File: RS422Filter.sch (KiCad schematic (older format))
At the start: 26 parts

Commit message: start placement
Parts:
- C27, C28, C29, C30, C31, C32, C33, C34: renamed from C?; footprint (none) -> Capacitor_SMD:C_0603_1608Metric
- D19, D20: renamed from D?; footprint (none) -> Package_TO_SOT_SMD:SOT-23
- R61, R62, R63, R64, R65, R66: renamed from R?; footprint (none) -> Resistor_SMD:R_0603_1608Metric
- gave numbers to parts that had none: 10

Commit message: placement
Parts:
- removed C29, C30: 470p, Capacitor_SMD:C_0603_1608Metric, symbol AR2ISS:C
- removed C33, C34: 1n, Capacitor_SMD:C_0603_1608Metric, symbol AR2ISS:C
- removed D20: PESD2CAN, Package_TO_SOT_SMD:SOT-23, symbol Device:D_TVS_x2_AAC
- removed J13: Conn_01x02, symbol Connector_Generic:Conn_01x02
- removed L12, L13: 10u, symbol Device:L
- removed L16, L17: 74279266, symbol Device:L
- removed R63, R64: 221, Resistor_SMD:R_0603_1608Metric, symbol AR2ISS:R
- removed R66: 120, Resistor_SMD:R_0603_1608Metric, symbol AR2ISS:R
- D19: footprint Package_TO_SOT_SMD:SOT-23 -> Package_TO_SOT_SMD:SOT-23_Handsoldering
- J12: footprint (none) -> Connector_PinHeader_2.54mm:PinHeader_1x02_P2.54mm_Vertical
- L14, L15: footprint (none) -> Inductor_SMD:L_0603_1608Metric
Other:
- moved on the sheet: C14, C15, C18, C19, D17, J9, L1, L2, L5, L6, R36, R37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

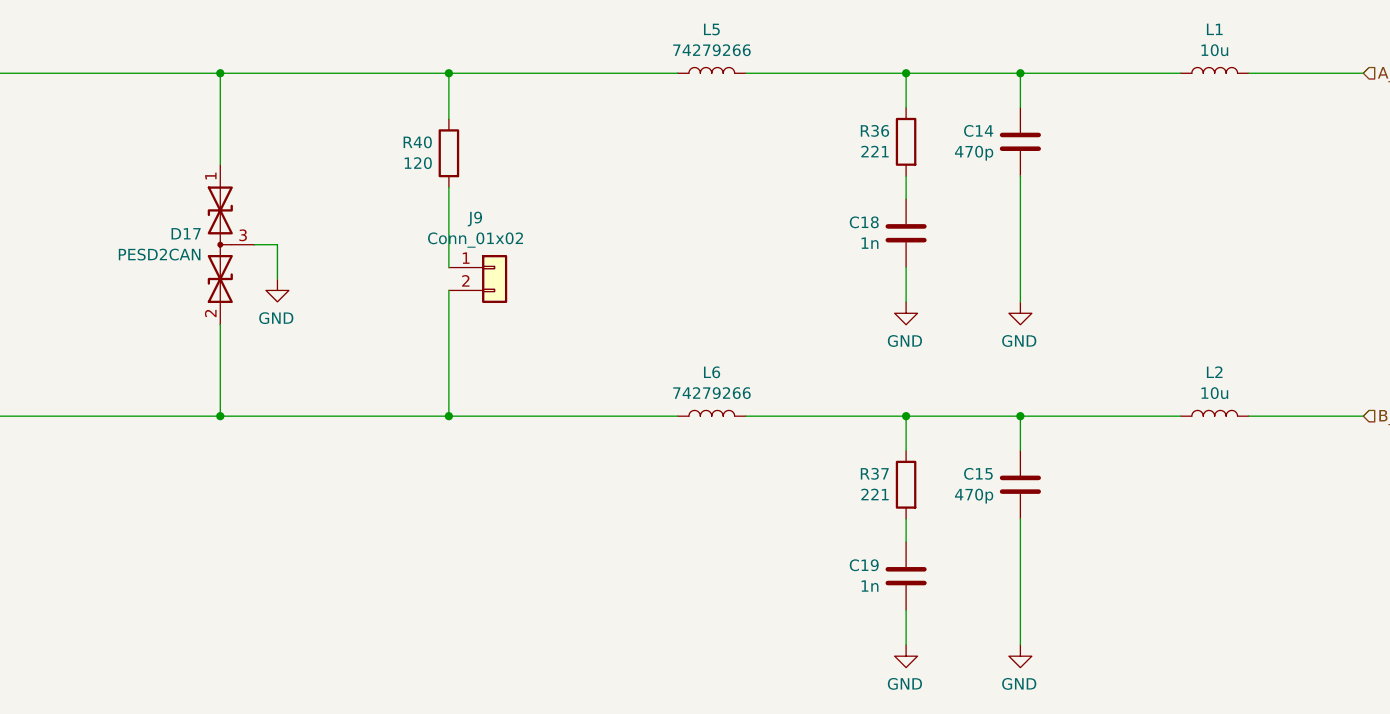
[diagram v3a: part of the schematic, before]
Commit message: add TLE5602
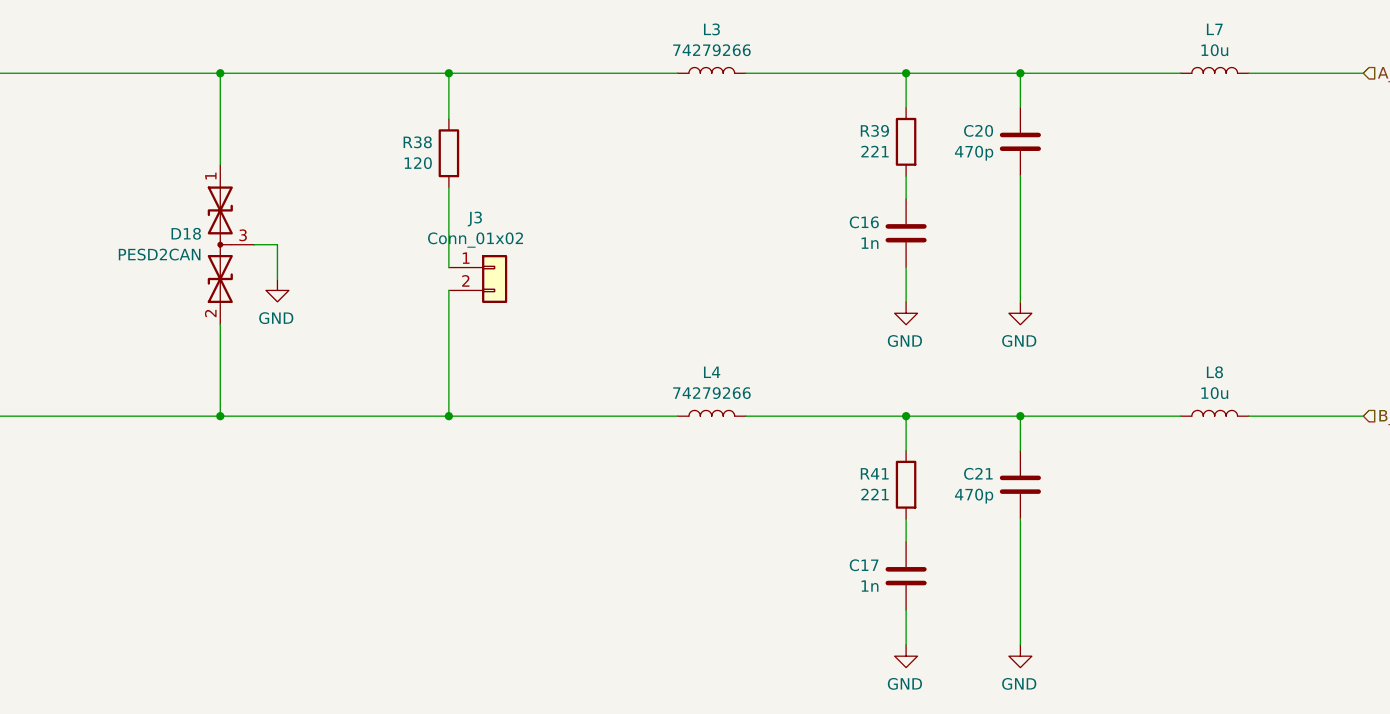
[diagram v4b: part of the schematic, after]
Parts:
- L10, L11: footprint (none) -> Inductor_SMD:L_0603_1608Metric
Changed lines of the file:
@@
 AR Path="/6089ADE2/608D0C52/608D8603" Ref="D?"  Part="1"
 AR Path="/6089ADE2/608DD62D/608D8603" Ref="D18"  Part="1"
-F 0 "D17" V 3404 3330 50  0000 L CNN
+F 0 "D18" V 3404 3330 50  0000 L CNN
 F 1 "PESD2CAN" V 3495 3330 50  0000 L CNN
 F 2 "Package_TO_SOT_SMD:SOT-23_Handsoldering" H 3300 3250 50  0001 C CNN
@@
 AR Path="/6089ADE2/608D0C52/608D8609" Ref="L?"  Part="1"
 AR Path="/6089ADE2/608DD62D/608D8609" Ref="L3"  Part="1"
-F 0 "L5" V 5790 2500 50  0000 C CNN
+F 0 "L3" V 5790 2500 50  0000 C CNN
 F 1 "74279266" V 5699 2500 50  0000 C CNN
 F 2 "Inductor_SMD:L_0603_1608Metric" H 5600 2500 50  0001 C CNN
@@
 AR Path="/6089ADE2/608D0C52/608D985F" Ref="R?"  Part="1"
 AR Path="/6089ADE2/608DD62D/608D985F" Ref="R39"  Part="1"
-F 0 "R36" H 6520 2846 50  0000 L CNN
+F 0 "R39" H 6520 2846 50  0000 L CNN
 F 1 "221" H 6520 2755 50  0000 L CNN
 F 2 "Resistor_SMD:R_0603_1608Metric" V 6380 2800 50  0001 C CNN
@@
 AR Path="/6089ADE2/608D0C52/608D9BE8" Ref="C?"  Part="1"
 AR Path="/6089ADE2/608DD62D/608D9BE8" Ref="C16"  Part="1"
-F 0 "C18" H 6565 3246 50  0000 L CNN
+F 0 "C16" H 6565 3246 50  0000 L CNN
 F 1 "1n" H 6565 3155 50  0000 L CNN
 F 2 "Capacitor_SMD:C_0603_1608Metric" H 6488 3050 50  0001 C CNN
@@
 AR Path="/6089ADE2/608D0C52/608DA048" Ref="C?"  Part="1"
 AR Path="/6089ADE2/608DD62D/608DA048" Ref="C20"  Part="1"
-F 0 "C14" H 7065 2846 50  0000 L CNN
+F 0 "C20" H 7065 2846 50  0000 L CNN
 F 1 "470p" H 7065 2755 50  0000 L CNN
 F 2 "Capacitor_SMD:C_0603_1608Metric" H 6988 2650 50  0001 C CNN
@@
 AR Path="/6089ADE2/608D0C52/608DA55F" Ref="L?"  Part="1"
 AR Path="/6089ADE2/608DD62D/608DA55F" Ref="L7"  Part="1"
-F 0 "L1" V 7990 2500 50  0000 C CNN
+F 0 "L7" V 7990 2500 50  0000 C CNN
 F 1 "10u" V 7899 2500 50  0000 C CNN
-F 2 "" H 7800 2500 50  0001 C CNN
+F 2 "Inductor_SMD:L_0603_1608Metric" H 7800 2500 50  0001 C CNN
 F 3 "~" H 7800 2500 50  0001 C CNN
 	1    7800 2500
@@
 AR Path="/6089ADE2/608D0C52/608E2FA4" Ref="L?"  Part="1"
 AR Path="/6089ADE2/608DD62D/608E2FA4" Ref="L4"  Part="1"
-F 0 "L6" V 5790 4000 50  0000 C CNN
+F 0 "L4" V 5790 4000 50  0000 C CNN
 F 1 "74279266" V 5699 4000 50  0000 C CNN
 F 2 "Inductor_SMD:L_0603_1608Metric" H 5600 4000 50  0001 C CNN
@@
 AR Path="/6089ADE2/608D0C52/608E2FAA" Ref="R?"  Part="1"
 AR Path="/6089ADE2/608DD62D/608E2FAA" Ref="R41"  Part="1"
-F 0 "R37" H 6520 4346 50  0000 L CNN
+F 0 "R41" H 6520 4346 50  0000 L CNN
 F 1 "221" H 6520 4255 50  0000 L CNN
 F 2 "Resistor_SMD:R_0603_1608Metric" V 6380 4300 50  0001 C CNN
@@
 AR Path="/6089ADE2/608D0C52/608E2FB0" Ref="C?"  Part="1"
 AR Path="/6089ADE2/608DD62D/608E2FB0" Ref="C17"  Part="1"
-F 0 "C19" H 6565 4746 50  0000 L CNN
+F 0 "C17" H 6565 4746 50  0000 L CNN
 F 1 "1n" H 6565 4655 50  0000 L CNN
 F 2 "Capacitor_SMD:C_0603_1608Metric" H 6488 4550 50  0001 C CNN
@@
 AR Path="/6089ADE2/608D0C52/608E2FB6" Ref="C?"  Part="1"
 AR Path="/6089ADE2/608DD62D/608E2FB6" Ref="C21"  Part="1"
-F 0 "C15" H 7065 4346 50  0000 L CNN
+F 0 "C21" H 7065 4346 50  0000 L CNN
 F 1 "470p" H 7065 4255 50  0000 L CNN
 F 2 "Capacitor_SMD:C_0603_1608Metric" H 6988 4150 50  0001 C CNN
@@
 AR Path="/6089ADE2/608D0C52/608E2FBC" Ref="L?"  Part="1"
 AR Path="/6089ADE2/608DD62D/608E2FBC" Ref="L8"  Part="1"
-F 0 "L2" V 7990 4000 50  0000 C CNN
+F 0 "L8" V 7990 4000 50  0000 C CNN
 F 1 "10u" V 7899 4000 50  0000 C CNN
-F 2 "" H 7800 4000 50  0001 C CNN
+F 2 "Inductor_SMD:L_0603_1608Metric" H 7800 4000 50  0001 C CNN
 F 3 "~" H 7800 4000 50  0001 C CNN
 	1    7800 4000
@@
 AR Path="/6089ADE2/608D0C52/609E589E" Ref="R?"  Part="1"
 AR Path="/6089ADE2/608DD62D/609E589E" Ref="R38"  Part="1"
-F 0 "R40" H 4520 2896 50  0000 L CNN
+F 0 "R38" H 4520 2896 50  0000 L CNN
 F 1 "120" H 4520 2805 50  0000 L CNN
 F 2 "Resistor_SMD:R_0603_1608Metric" V 4380 2850 50  0001 C CNN
@@
 AR Path="/6089ADE2/608D0C52/609E64E5" Ref="J?"  Part="1"
 AR Path="/6089ADE2/608DD62D/609E64E5" Ref="J3"  Part="1"
-F 0 "J9" H 4568 3567 50  0000 C CNN
+F 0 "J3" H 4568 3567 50  0000 C CNN
 F 1 "Conn_01x02" H 4568 3476 50  0000 C CNN
 F 2 "Connector_PinHeader_2.54mm:PinHeader_1x02_P2.54mm_Vertical" H 4650 3350 50  0001 C CNN

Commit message: routing
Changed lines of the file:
@@
 $Descr A4 11693 8268
 encoding utf-8
-Sheet 5 22
+Sheet 4 22
 Title ""
 Date ""
@@
 AR Path="/6089ADE2/608D0C52/608D8603" Ref="D?"  Part="1"
 AR Path="/6089ADE2/608DD62D/608D8603" Ref="D18"  Part="1"
-F 0 "D18" V 3404 3330 50  0000 L CNN
+F 0 "D17" V 3404 3330 50  0000 L CNN
 F 1 "PESD2CAN" V 3495 3330 50  0000 L CNN
 F 2 "Package_TO_SOT_SMD:SOT-23_Handsoldering" H 3300 3250 50  0001 C CNN
@@
 AR Path="/6089ADE2/608D0C52/608D8609" Ref="L?"  Part="1"
 AR Path="/6089ADE2/608DD62D/608D8609" Ref="L3"  Part="1"
-F 0 "L3" V 5790 2500 50  0000 C CNN
+F 0 "L5" V 5790 2500 50  0000 C CNN
 F 1 "74279266" V 5699 2500 50  0000 C CNN
 F 2 "Inductor_SMD:L_0603_1608Metric" H 5600 2500 50  0001 C CNN
@@
 AR Path="/6089ADE2/608D0C52/608D985F" Ref="R?"  Part="1"
 AR Path="/6089ADE2/608DD62D/608D985F" Ref="R39"  Part="1"
-F 0 "R39" H 6520 2846 50  0000 L CNN
+F 0 "R36" H 6520 2846 50  0000 L CNN
 F 1 "221" H 6520 2755 50  0000 L CNN
 F 2 "Resistor_SMD:R_0603_1608Metric" V 6380 2800 50  0001 C CNN
@@
 AR Path="/6089ADE2/608D0C52/608D9BE8" Ref="C?"  Part="1"
 AR Path="/6089ADE2/608DD62D/608D9BE8" Ref="C16"  Part="1"
-F 0 "C16" H 6565 3246 50  0000 L CNN
+F 0 "C18" H 6565 3246 50  0000 L CNN
 F 1 "1n" H 6565 3155 50  0000 L CNN
 F 2 "Capacitor_SMD:C_0603_1608Metric" H 6488 3050 50  0001 C CNN
@@
 AR Path="/6089ADE2/608D0C52/608DA048" Ref="C?"  Part="1"
 AR Path="/6089ADE2/608DD62D/608DA048" Ref="C20"  Part="1"
-F 0 "C20" H 7065 2846 50  0000 L CNN
+F 0 "C14" H 7065 2846 50  0000 L CNN
 F 1 "470p" H 7065 2755 50  0000 L CNN
 F 2 "Capacitor_SMD:C_0603_1608Metric" H 6988 2650 50  0001 C CNN
@@
 AR Path="/6089ADE2/608D0C52/608DA55F" Ref="L?"  Part="1"
 AR Path="/6089ADE2/608DD62D/608DA55F" Ref="L7"  Part="1"
-F 0 "L7" V 7990 2500 50  0000 C CNN
+F 0 "L1" V 7990 2500 50  0000 C CNN
 F 1 "10u" V 7899 2500 50  0000 C CNN
 F 2 "Inductor_SMD:L_0603_1608Metric" H 7800 2500 50  0001 C CNN
@@
 AR Path="/6089ADE2/608D0C52/608DBE73" Ref="#PWR?"  Part="1"
 AR Path="/6089ADE2/608DD62D/608DBE73" Ref="#PWR0203"  Part="1"
-F 0 "#PWR0203" H 6450 3250 50  0001 C CNN
+F 0 "#PWR047" H 6450 3250 50  0001 C CNN
 F 1 "GND" H 6455 3327 50  0000 C CNN
 F 2 "" H 6450 3500 50  0001 C CNN
@@
 AR Path="/6089ADE2/608D0C52/608DC4B4" Ref="#PWR?"  Part="1"
 AR Path="/6089ADE2/608DD62D/608DC4B4" Ref="#PWR0204"  Part="1"
-F 0 "#PWR0204" H 6950 3250 50  0001 C CNN
+F 0 "#PWR043" H 6950 3250 50  0001 C CNN
 F 1 "GND" H 6955 3327 50  0000 C CNN
 F 2 "" H 6950 3500 50  0001 C CNN
@@
 AR Path="/6089ADE2/608D0C52/608E2FA4" Ref="L?"  Part="1"
 AR Path="/6089ADE2/608DD62D/608E2FA4" Ref="L4"  Part="1"
-F 0 "L4" V 5790 4000 50  0000 C CNN
+F 0 "L6" V 5790 4000 50  0000 C CNN
 F 1 "74279266" V 5699 4000 50  0000 C CNN
 F 2 "Inductor_SMD:L_0603_1608Metric" H 5600 4000 50  0001 C CNN
@@
 AR Path="/6089ADE2/608D0C52/608E2FAA" Ref="R?"  Part="1"
 AR Path="/6089ADE2/608DD62D/608E2FAA" Ref="R41"  Part="1"
-F 0 "R41" H 6520 4346 50  0000 L CNN
+F 0 "R37" H 6520 4346 50  0000 L CNN
 F 1 "221" H 6520 4255 50  0000 L CNN
 F 2 "Resistor_SMD:R_0603_1608Metric" V 6380 4300 50  0001 C CNN
@@
 AR Path="/6089ADE2/608D0C52/608E2FB0" Ref="C?"  Part="1"
 AR Path="/6089ADE2/608DD62D/608E2FB0" Ref="C17"  Part="1"
-F 0 "C17" H 6565 4746 50  0000 L CNN
+F 0 "C19" H 6565 4746 50  0000 L CNN
 F 1 "1n" H 6565 4655 50  0000 L CNN
 F 2 "Capacitor_SMD:C_0603_1608Metric" H 6488 4550 50  0001 C CNN
@@
 AR Path="/6089ADE2/608D0C52/608E2FB6" Ref="C?"  Part="1"
 AR Path="/6089ADE2/608DD62D/608E2FB6" Ref="C21"  Part="1"
-F 0 "C21" H 7065 4346 50  0000 L CNN
+F 0 "C15" H 7065 4346 50  0000 L CNN
 F 1 "470p" H 7065 4255 50  0000 L CNN
 F 2 "Capacitor_SMD:C_0603_1608Metric" H 6988 4150 50  0001 C CNN
@@
 AR Path="/6089ADE2/608D0C52/608E2FBC" Ref="L?"  Part="1"
 AR Path="/6089ADE2/608DD62D/608E2FBC" Ref="L8"  Part="1"
-F 0 "L8" V 7990 4000 50  0000 C CNN
+F 0 "L2" V 7990 4000 50  0000 C CNN
 F 1 "10u" V 7899 4000 50  0000 C CNN
 F 2 "Inductor_SMD:L_0603_1608Metric" H 7800 4000 50  0001 C CNN
@@
 AR Path="/6089ADE2/608D0C52/608E2FC6" Ref="#PWR?"  Part="1"
 AR Path="/6089ADE2/608DD62D/608E2FC6" Ref="#PWR0205"  Part="1"
-F 0 "#PWR0205" H 6450 4750 50  0001 C CNN
+F 0 "#PWR048" H 6450 4750 50  0001 C CNN
 F 1 "GND" H 6455 4827 50  0000 C CNN
 F 2 "" H 6450 5000 50  0001 C CNN
@@
 AR Path="/6089ADE2/608D0C52/608E2FCD" Ref="#PWR?"  Part="1"
 AR Path="/6089ADE2/608DD62D/608E2FCD" Ref="#PWR0206"  Part="1"
-F 0 "#PWR0206" H 6950 4750 50  0001 C CNN
+F 0 "#PWR044" H 6950 4750 50  0001 C CNN
 F 1 "GND" H 6955 4827 50  0000 C CNN
 F 2 "" H 6950 5000 50  0001 C CNN
@@
 AR Path="/6089ADE2/608D0C52/608E4369" Ref="#PWR?"  Part="1"
 AR Path="/6089ADE2/608DD62D/608E4369" Ref="#PWR0207"  Part="1"
-F 0 "#PWR0207" H 3700 3150 50  0001 C CNN
+F 0 "#PWR051" H 3700 3150 50  0001 C CNN
 F 1 "GND" H 3705 3227 50  0000 C CNN
 F 2 "" H 3700 3400 50  0001 C CNN
@@
 AR Path="/6089ADE2/608D0C52/609E589E" Ref="R?"  Part="1"
 AR Path="/6089ADE2/608DD62D/609E589E" Ref="R38"  Part="1"
-F 0 "R38" H 4520 2896 50  0000 L CNN
+F 0 "R40" H 4520 2896 50  0000 L CNN
 F 1 "120" H 4520 2805 50  0000 L CNN
 F 2 "Resistor_SMD:R_0603_1608Metric" V 4380 2850 50  0001 C CNN
@@
 AR Path="/6089ADE2/608D0C52/609E64E5" Ref="J?"  Part="1"
 AR Path="/6089ADE2/608DD62D/609E64E5" Ref="J3"  Part="1"
-F 0 "J3" H 4568 3567 50  0000 C CNN
+F 0 "J9" H 4568 3567 50  0000 C CNN
 F 1 "Conn_01x02" H 4568 3476 50  0000 C CNN
 F 2 "Connector_PinHeader_2.54mm:PinHeader_1x02_P2.54mm_Vertical" H 4650 3350 50  0001 C CNN

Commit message: placement, routing
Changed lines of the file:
@@
 $Descr A4 11693 8268
 encoding utf-8
-Sheet 4 22
+Sheet 5 22
 Title ""
 Date ""
@@
 AR Path="/6089ADE2/608D0C52/608D8603" Ref="D?"  Part="1"
 AR Path="/6089ADE2/608DD62D/608D8603" Ref="D18"  Part="1"
-F 0 "D17" V 3404 3330 50  0000 L CNN
+F 0 "D18" V 3404 3330 50  0000 L CNN
 F 1 "PESD2CAN" V 3495 3330 50  0000 L CNN
 F 2 "Package_TO_SOT_SMD:SOT-23_Handsoldering" H 3300 3250 50  0001 C CNN
@@
 AR Path="/6089ADE2/608D0C52/608D8609" Ref="L?"  Part="1"
 AR Path="/6089ADE2/608DD62D/608D8609" Ref="L3"  Part="1"
-F 0 "L5" V 5790 2500 50  0000 C CNN
+F 0 "L3" V 5790 2500 50  0000 C CNN
 F 1 "74279266" V 5699 2500 50  0000 C CNN
 F 2 "Inductor_SMD:L_0603_1608Metric" H 5600 2500 50  0001 C CNN
@@
 AR Path="/6089ADE2/608D0C52/608D985F" Ref="R?"  Part="1"
 AR Path="/6089ADE2/608DD62D/608D985F" Ref="R39"  Part="1"
-F 0 "R36" H 6520 2846 50  0000 L CNN
+F 0 "R39" H 6520 2846 50  0000 L CNN
 F 1 "221" H 6520 2755 50  0000 L CNN
 F 2 "Resistor_SMD:R_0603_1608Metric" V 6380 2800 50  0001 C CNN
@@
 AR Path="/6089ADE2/608D0C52/608D9BE8" Ref="C?"  Part="1"
 AR Path="/6089ADE2/608DD62D/608D9BE8" Ref="C16"  Part="1"
-F 0 "C18" H 6565 3246 50  0000 L CNN
+F 0 "C16" H 6565 3246 50  0000 L CNN
 F 1 "1n" H 6565 3155 50  0000 L CNN
 F 2 "Capacitor_SMD:C_0603_1608Metric" H 6488 3050 50  0001 C CNN
@@
 AR Path="/6089ADE2/608D0C52/608DA048" Ref="C?"  Part="1"
 AR Path="/6089ADE2/608DD62D/608DA048" Ref="C20"  Part="1"
-F 0 "C14" H 7065 2846 50  0000 L CNN
+F 0 "C20" H 7065 2846 50  0000 L CNN
 F 1 "470p" H 7065 2755 50  0000 L CNN
 F 2 "Capacitor_SMD:C_0603_1608Metric" H 6988 2650 50  0001 C CNN
@@
 AR Path="/6089ADE2/608D0C52/608DA55F" Ref="L?"  Part="1"
 AR Path="/6089ADE2/608DD62D/608DA55F" Ref="L7"  Part="1"
-F 0 "L1" V 7990 2500 50  0000 C CNN
+F 0 "L7" V 7990 2500 50  0000 C CNN
 F 1 "10u" V 7899 2500 50  0000 C CNN
 F 2 "Inductor_SMD:L_0603_1608Metric" H 7800 2500 50  0001 C CNN
@@
 AR Path="/6089ADE2/608D0C52/608E2FA4" Ref="L?"  Part="1"
 AR Path="/6089ADE2/608DD62D/608E2FA4" Ref="L4"  Part="1"
-F 0 "L6" V 5790 4000 50  0000 C CNN
+F 0 "L4" V 5790 4000 50  0000 C CNN
 F 1 "74279266" V 5699 4000 50  0000 C CNN
 F 2 "Inductor_SMD:L_0603_1608Metric" H 5600 4000 50  0001 C CNN
@@
 AR Path="/6089ADE2/608D0C52/608E2FAA" Ref="R?"  Part="1"
 AR Path="/6089ADE2/608DD62D/608E2FAA" Ref="R41"  Part="1"
-F 0 "R37" H 6520 4346 50  0000 L CNN
+F 0 "R41" H 6520 4346 50  0000 L CNN
 F 1 "221" H 6520 4255 50  0000 L CNN
 F 2 "Resistor_SMD:R_0603_1608Metric" V 6380 4300 50  0001 C CNN
@@
 AR Path="/6089ADE2/608D0C52/608E2FB0" Ref="C?"  Part="1"
 AR Path="/6089ADE2/608DD62D/608E2FB0" Ref="C17"  Part="1"
-F 0 "C19" H 6565 4746 50  0000 L CNN
+F 0 "C17" H 6565 4746 50  0000 L CNN
 F 1 "1n" H 6565 4655 50  0000 L CNN
 F 2 "Capacitor_SMD:C_0603_1608Metric" H 6488 4550 50  0001 C CNN
@@
 AR Path="/6089ADE2/608D0C52/608E2FB6" Ref="C?"  Part="1"
 AR Path="/6089ADE2/608DD62D/608E2FB6" Ref="C21"  Part="1"
-F 0 "C15" H 7065 4346 50  0000 L CNN
+F 0 "C21" H 7065 4346 50  0000 L CNN
 F 1 "470p" H 7065 4255 50  0000 L CNN
 F 2 "Capacitor_SMD:C_0603_1608Metric" H 6988 4150 50  0001 C CNN
@@
 AR Path="/6089ADE2/608D0C52/608E2FBC" Ref="L?"  Part="1"
 AR Path="/6089ADE2/608DD62D/608E2FBC" Ref="L8"  Part="1"
-F 0 "L2" V 7990 4000 50  0000 C CNN
+F 0 "L8" V 7990 4000 50  0000 C CNN
 F 1 "10u" V 7899 4000 50  0000 C CNN
 F 2 "Inductor_SMD:L_0603_1608Metric" H 7800 4000 50  0001 C CNN
@@
 AR Path="/6089ADE2/608D0C52/609E589E" Ref="R?"  Part="1"
 AR Path="/6089ADE2/608DD62D/609E589E" Ref="R38"  Part="1"
-F 0 "R40" H 4520 2896 50  0000 L CNN
+F 0 "R38" H 4520 2896 50  0000 L CNN
 F 1 "120" H 4520 2805 50  0000 L CNN
 F 2 "Resistor_SMD:R_0603_1608Metric" V 4380 2850 50  0001 C CNN
@@
 AR Path="/6089ADE2/608D0C52/609E64E5" Ref="J?"  Part="1"
 AR Path="/6089ADE2/608DD62D/609E64E5" Ref="J3"  Part="1"
-F 0 "J9" H 4568 3567 50  0000 C CNN
+F 0 "J3" H 4568 3567 50  0000 C CNN
 F 1 "Conn_01x02" H 4568 3476 50  0000 C CNN
 F 2 "Connector_PinHeader_2.54mm:PinHeader_1x02_P2.54mm_Vertical" H 4650 3350 50  0001 C CNN
